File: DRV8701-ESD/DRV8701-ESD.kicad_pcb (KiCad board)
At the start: 2 copper layers, 61 parts, among them J1 V_Main, J10 POT_signal, J11 GND, J12 Conn_01x05_Pin, J2 V_OUT -, J3 V_OUT +, J4 CW, J5 OFF, J6 CCW, J7 MAIN TRIGGER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

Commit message: Some Routing done
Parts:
- added R7: 5m, Resistor_SMD:R_2512_6332Metric_Pad1.40x3.35mm_HandSolder, F.Cu at (252.6, 52.8)
- added U1: DRV8701ERGER, DRV8701:RGE0024F_NV, F.Cu at (154.2, 69.9)
- C16, C17: footprint Capacitor_SMD:C_0805_2012Metric_Pad1.18x1.45mm_HandSolder -> Capacitor_SMD:C_1210_3225Metric_Pad1.33x2.70mm_HandSolder
- moved C14 180.5 mm to (261.2, 67.4)
- moved C6 180.5 mm to (261.2, 60.7)
- moved C7 180.5 mm to (261.2, 64.0)
- moved D1 156.3 mm to (264.5, 51.7)
- moved U2 153.8 mm to (259.7, 52.8)
- moved C17 152.8 mm to (262.7, 88.8)
- moved C16 152.6 mm to (262.7, 84.5)
- moved L1 149.6 mm to (262.5, 73.0)
- moved C10 149.6 mm to (240.5, 91.2)
- moved C11 149.6 mm to (240.5, 93.7)
- moved C12 149.6 mm to (240.5, 96.2)
- moved C13 149.6 mm to (240.5, 98.7)
- moved C15 149.6 mm to (240.5, 101.2)
- moved J10 149.6 mm to (264.1, 43.5)
- moved J11 149.6 mm to (264.1, 48.1)
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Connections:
- D2 pad 1: /VCC -> +12V
- D2 pad 2: +12V -> /VCC
- D2 pad 3: (no net) -> +12V
- D3 pad 1: /VCC -> +12V
- D3 pad 2: +12V -> /VCC
- D3 pad 3: (no net) -> +12V
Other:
- board outline added: 55 x 95 mm

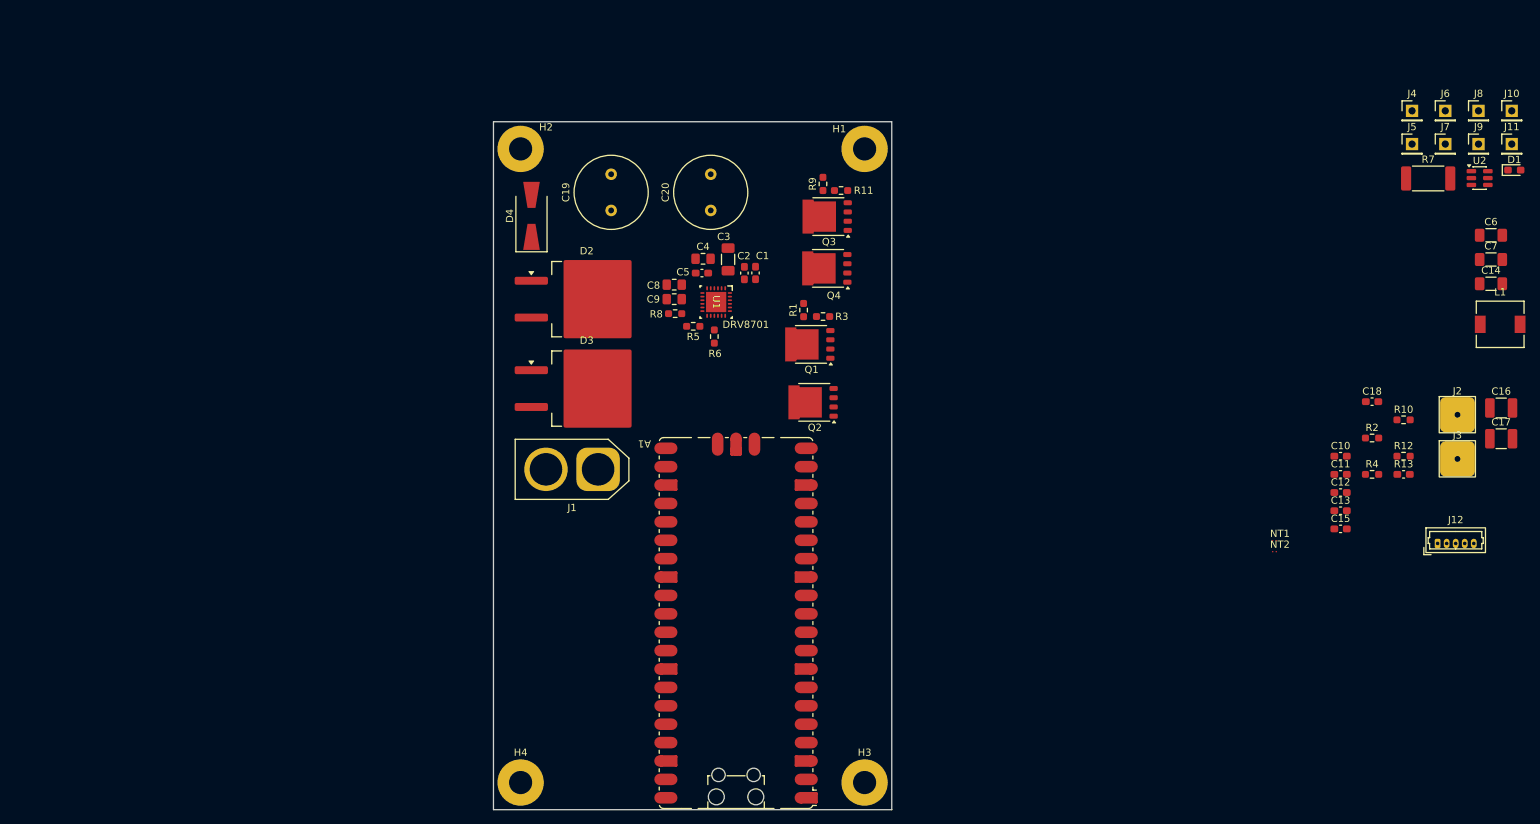
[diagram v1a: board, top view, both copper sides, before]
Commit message: Component Placement - Tentative
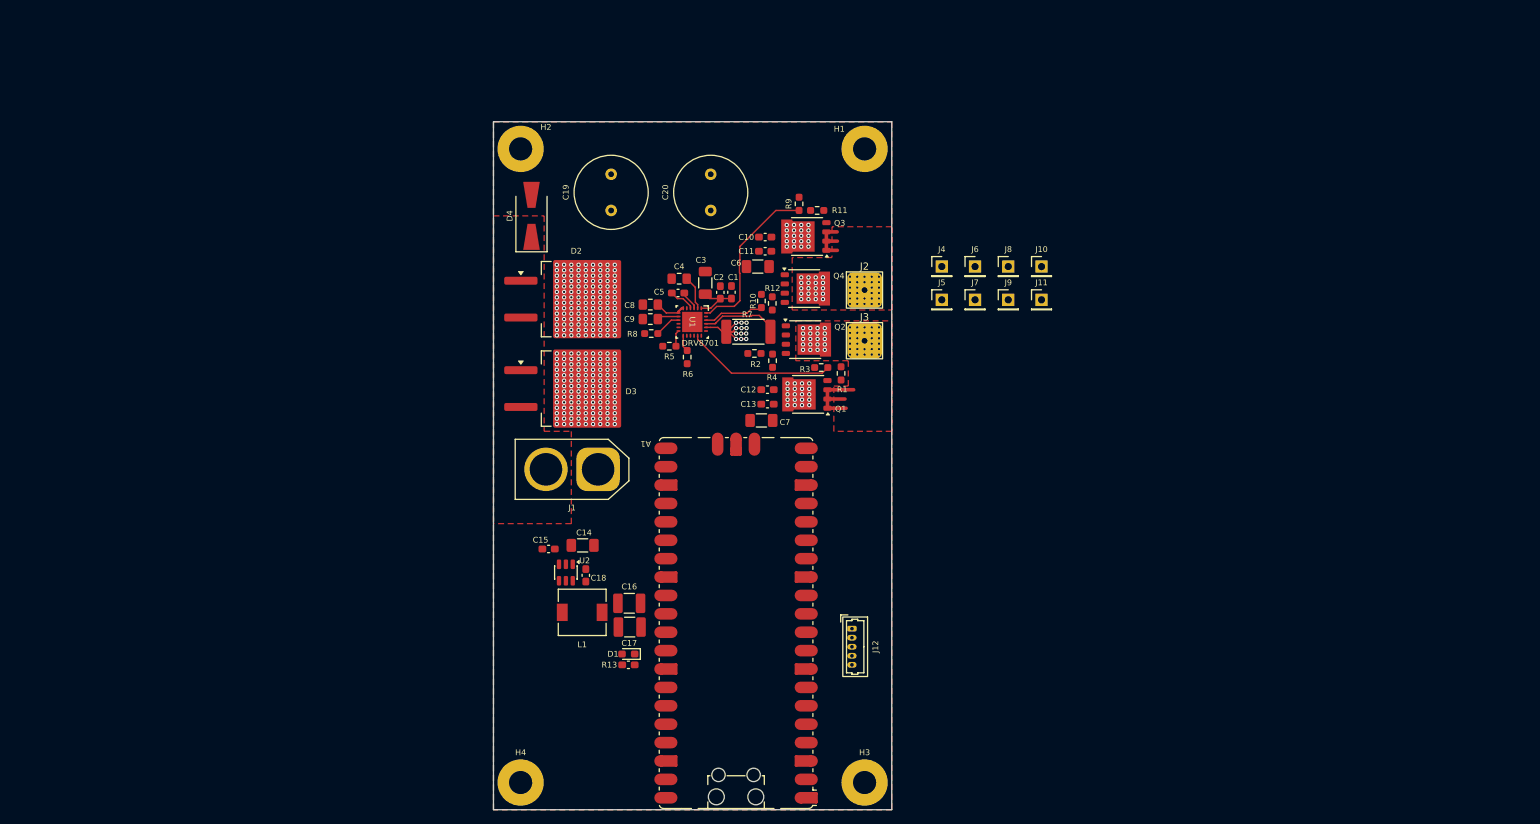
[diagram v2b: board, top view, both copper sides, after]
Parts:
- NT1, NT2: footprint Net_Ties:NetTie_0.2mm_SMD -> Net_Ties:NetTie-2_SMD_Pad0.2mm
- moved D1 139.4 mm to (142.1, 118.5), turned to 180 degrees
- moved U2 137.4 mm to (133.5, 107.2), turned to -90 degrees
- moved L1 132.9 mm to (135.8, 112.8), turned to 180 degrees
- moved C14 130.5 mm to (135.8, 103.5), turned to 180 degrees
- moved C16 123.4 mm to (142.2, 111.5)
- moved C17 123.1 mm to (142.3, 114.8)
- moved C18 111.2 mm to (136.2, 107.6), turned to -90 degrees
- moved R13 110.2 mm to (142.1, 120.0)
- moved C15 109.4 mm to (131.1, 104.0), turned to 180 degrees
- moved C7 103.2 mm to (160.5, 86.2)
- moved C6 101.3 mm to (160.0, 65.0)
- moved R7 96.2 mm to (158.7, 74.0), turned to 180 degrees
- moved R10 90.2 mm to (160.5, 69.8), turned to 90 degrees
- moved R12 89.7 mm to (162.0, 70.1), turned to -90 degrees
- moved R2 86.1 mm to (159.5, 77.0)
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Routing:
- net /GH2: track 0.00 -> 23.1 mm
- net /GH1: track 0.00 -> 20.7 mm
- net GND: track 0.00 -> 13.7 mm, vias 0 -> 12
- net MOTOR+: track 0.00 -> 11.2 mm, vias 0 -> 48
- net /GL2: track 0.00 -> 8.37 mm
- net /VCC: track 0.00 -> 7.39 mm, vias 0 -> 292
- net MOTOR-: track 0.00 -> 7.07 mm, vias 0 -> 48
- net /SP: track 0.00 -> 6.83 mm
- net /VCP: track 0.00 -> 4.70 mm
- net /AVDD: track 0.00 -> 4.36 mm
- net /CPL: track 0.00 -> 3.62 mm
- net /nFAULT: track 0.00 -> 3.62 mm
- net /DVDD: track 0.00 -> 2.99 mm
- net /SP_TOP: track 0.00 -> 2.89 mm
- net /CPH: track 0.00 -> 2.66 mm
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- added copper zone on F.Cu, net +12V
- added copper zone on B.Cu, net GND
- added copper zone on F.Cu, net GND
- added copper zone on F.Cu, net MOTOR+
- added copper zone on F.Cu, net MOTOR-

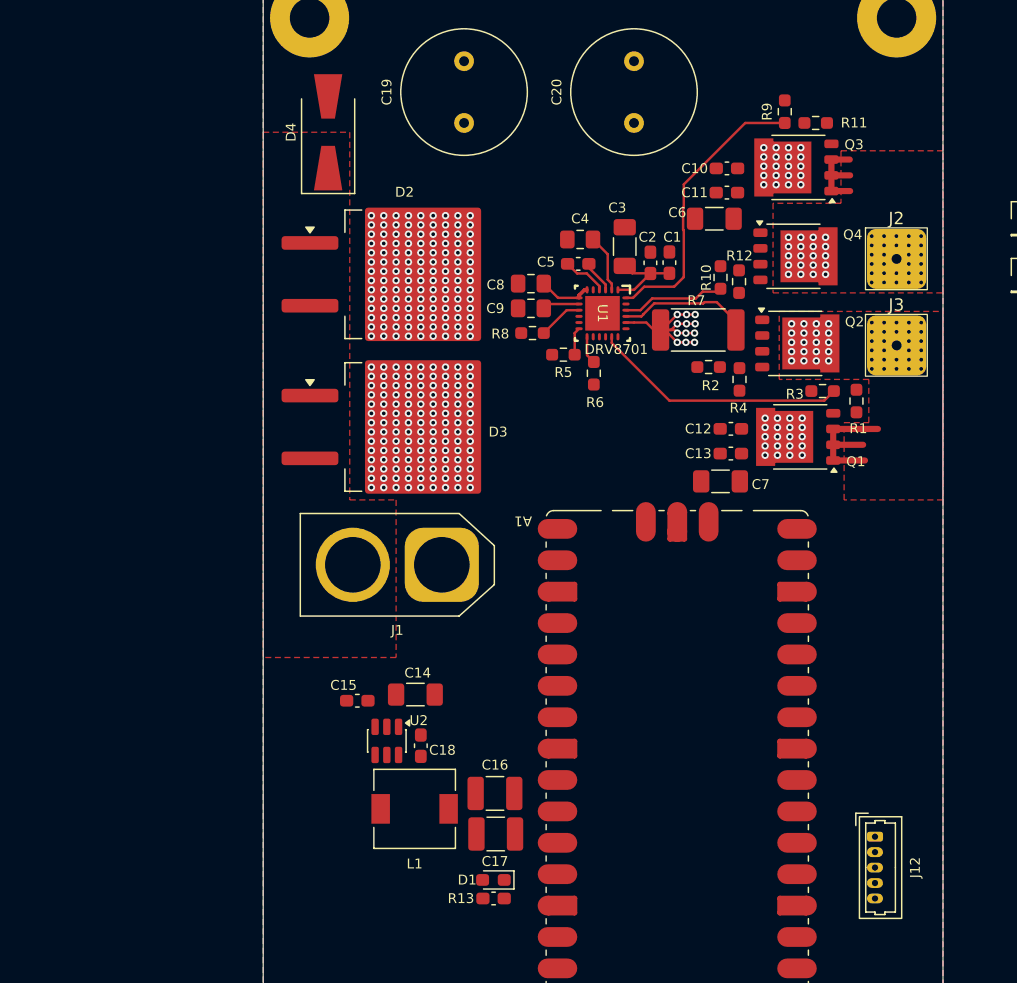
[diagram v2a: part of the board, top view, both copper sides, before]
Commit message: Added PMOS, Changed VREF to 3v3, Added 5->3v3 LDO, Placed components tentatively. Yet to review.
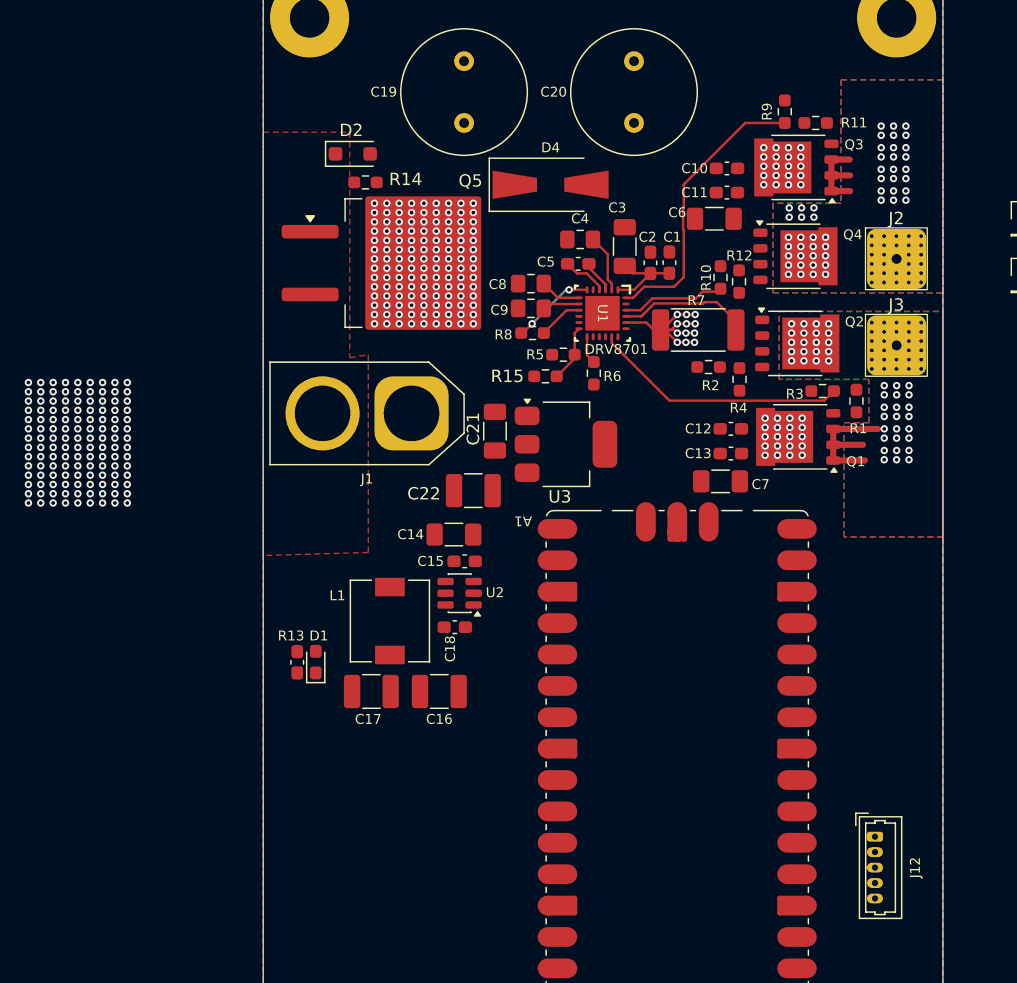
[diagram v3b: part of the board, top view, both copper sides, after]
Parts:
- removed D3: RBR10N, Package_TO_SOT_SMD:TO-263-2
- added C21: 10u, Capacitor_SMD:C_1206_3216Metric_Pad1.33x1.80mm_HandSolder, F.Cu at (142.2, 82.2)
- added C22: 22u, Capacitor_SMD:C_1210_3225Metric_Pad1.33x2.70mm_HandSolder, F.Cu at (140.5, 87.0)
- added Q5: IPB80P04P4L08ATMA2, Package_TO_SOT_SMD:TO-263-2, F.Cu at (134.9, 68.6)
- added R14: 100k, Resistor_SMD:R_0603_1608Metric_Pad0.98x0.95mm_HandSolder, F.Cu at (131.8, 62.1)
- added R15: 33k, Resistor_SMD:R_0603_1608Metric_Pad0.98x0.95mm_HandSolder, F.Cu at (146.3, 77.8)
- added U3: AZ1117CH2-3.3, Package_TO_SOT_SMD:SOT-223-3_TabPin2, F.Cu at (148.0, 83.2)
- D2: value RBR10N -> BZT52C12; footprint Package_TO_SOT_SMD:TO-263-2 -> Diode_SMD:D_SOD-123F
- moved R13 24.9 mm to (126.2, 100.9), turned to -90 degrees
- moved D1 22.7 mm to (127.8, 100.9), turned to 90 degrees
- moved D4 18.5 mm to (146.8, 62.2), turned to 0 degrees
- moved L1 15.3 mm to (133.8, 97.5), turned to 90 degrees
- moved C17 15.3 mm to (132.2, 103.2), turned to 180 degrees
- moved C15 14.2 mm to (139.8, 92.7)
- moved U2 13.3 mm to (139.4, 95.3), turned to 180 degrees
- moved C14 13.3 mm to (138.9, 90.6), turned to 0 degrees
- moved J1 12.5 mm to (135.5, 80.8)
- moved D2 10.6 mm to (130.8, 59.8)
- moved C18 9.97 mm to (139.0, 98.0), turned to 180 degrees
- moved C16 9.40 mm to (137.8, 103.2)
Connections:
- A1 pad 36: +3V3 -> unconnected-(A1-3V3-Pad36)
- D2 pad 2: /VCC -> Net-(D2-A)
- D4 pad 1: +12V -> /VCC
- U1 pad 6: /AVDD -> +3V3
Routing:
- net +3V3: track 0.00 -> 6.77 mm, vias 0 -> 2
- net /IDRIVE: track 2.24 -> 4.60 mm
- net /AVDD: track 4.36 -> 3.33 mm
- net MOTOR-: vias 48 -> 78
- net MOTOR+: vias 48 -> 72
- added copper zone on B.Cu, net MOTOR+
- added copper zone on B.Cu, net MOTOR-

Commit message: Some layout changes
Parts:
- moved U3 0.50 mm to (148.0, 83.8)
- moved C4 0.39 mm to (148.8, 66.7)
- turned R1 to -90 degrees
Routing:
- net /VCC: track 7.39 -> 52.1 mm, vias 292 -> 300
- net /GL1: track 0.00 -> 7.26 mm
- net /SP_TOP: track 2.89 -> 7.99 mm
- net /GH1: track 20.7 -> 25.6 mm, vias 0 -> 2
- net Net-(Q2-G): track 0.00 -> 2.68 mm
- net Net-(Q1-G): track 0.00 -> 2.53 mm
- net /GH2: track 23.1 -> 20.9 mm, vias 0 -> 2
- net Net-(Q4-G): track 0.00 -> 2.05 mm
- net Net-(Q3-G): track 0.00 -> 1.84 mm
- net GND: track 13.7 -> 14.8 mm, vias 12 -> 29
- net MOTOR-: track 7.07 -> 8.05 mm, vias 78 -> 79
- added copper zone on B.Cu, net /VCC
- added copper zone on F.Cu, net /VCC

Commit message: Some more stuff added
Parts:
- added C23: 100n, Capacitor_SMD:C_0603_1608Metric_Pad1.08x0.95mm_HandSolder, F.Cu at (146.6, 74.5)
- added R16: 10k, Resistor_SMD:R_0603_1608Metric_Pad0.98x0.95mm_HandSolder, F.Cu at (146.0, 76.2)
- added R17: 20k, Resistor_SMD:R_0603_1608Metric_Pad0.98x0.95mm_HandSolder, F.Cu at (143.0, 114.5)
- added R18: 100k, Resistor_SMD:R_0603_1608Metric_Pad0.98x0.95mm_HandSolder, F.Cu at (142.2, 117.8)
- added R19: 100k, Resistor_SMD:R_0603_1608Metric_Pad0.98x0.95mm_HandSolder, F.Cu at (142.2, 120.0)
- moved R5 1.39 mm to (148.8, 77.0), turned to -90 degrees
- moved C8 1.25 mm to (145.2, 69.0)
- moved C9 1.25 mm to (145.2, 71.0)
- moved R8 1.25 mm to (145.4, 73.0)
- moved R6 0.50 mm to (150.8, 77.5)
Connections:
- A1 pad 31: /SO -> /SO_MCU
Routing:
- net /SO_MCU: track 0.00 -> 44.5 mm, vias 0 -> 2
- net /SO: track 0.00 -> 5.14 mm
- net GND: track 14.8 -> 17.6 mm, vias 29 -> 33
- net +3V3: track 6.77 -> 9.21 mm
- net /nFAULT: track 3.62 -> 3.01 mm
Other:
- copper layers 2 -> 4

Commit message: Changes done after review
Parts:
- removed C23: 100n, Capacitor_SMD:C_0603_1608Metric_Pad1.08x0.95mm_HandSolder
- L1: footprint Inductor_SMD:L_6.3x6.3_H3 -> Inductor_SMD_Custom:L_SMD_6mmx6mm
- moved R16 36.1 mm to (141.2, 112.0), turned to 90 degrees
- moved C22 35.2 mm to (131.2, 121.0)
- moved C21 31.0 mm to (126.8, 109.0)
- moved U3 30.1 mm to (133.8, 110.2)
- moved R8 28.9 mm to (142.2, 101.8), turned to 90 degrees
- moved R6 15.2 mm to (144.2, 91.2)
- moved L1 4.25 mm to (138.0, 97.8)
- moved NT2 2.88 mm to (156.8, 74.2), turned to 180 degrees
- moved NT1 2.73 mm to (161.2, 74.0)
- moved R10 2.41 mm to (158.8, 68.1), turned to -90 degrees
- moved R12 1.25 mm to (162.0, 68.8), turned to 90 degrees
- moved R7 0.39 mm to (159.0, 74.2)
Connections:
- U1 pad 6: +3V3 -> /AVDD
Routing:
- net /SO_MCU: track 44.5 -> 4.48 mm, vias 2 -> 1
- net /VCC: track 52.1 -> 19.7 mm
- net GND: track 17.6 -> 1.02 mm, vias 33 -> 17
- net /SN: track 0.65 -> 9.87 mm
- net +3V3: track 9.21 -> 0.00 mm, vias 2 -> 0
- net /SO: track 5.14 -> 0.00 mm
- net /nFAULT: track 3.01 -> 0.00 mm
- net /nSLEEP: track 2.71 -> 0.00 mm
- net /SP: track 6.83 -> 9.23 mm
- net /SP_TOP: track 7.99 -> 5.80 mm
- net Net-(Q4-G): track 2.05 -> 0.00 mm
- net /GL2: track 8.37 -> 7.29 mm
